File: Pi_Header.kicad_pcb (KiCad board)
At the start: 2 copper layers, 4 parts, among them J1 Raspberry_Pi_2_3, J2 UART, J3 I2C, U1 BD9F800MUX-ZE2

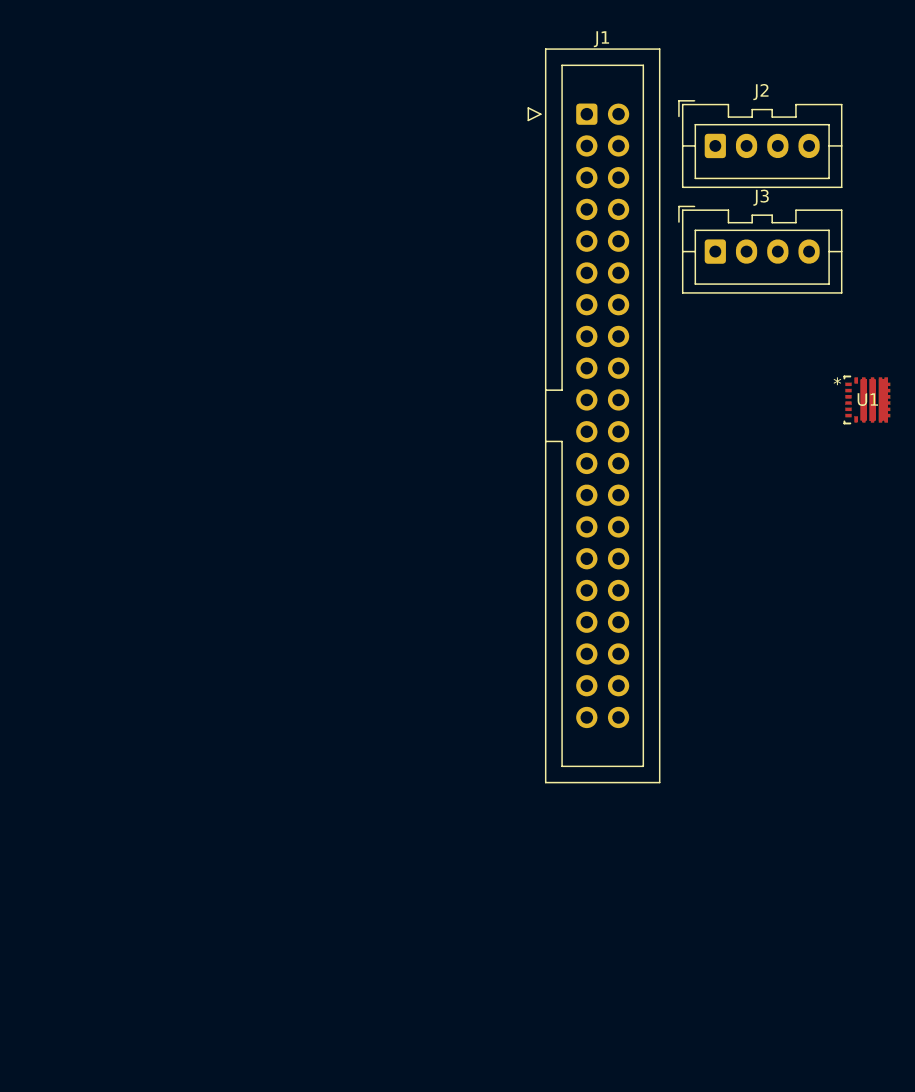
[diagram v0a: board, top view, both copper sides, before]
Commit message: スケッチ完成、PCBベタまで完成　あと外形
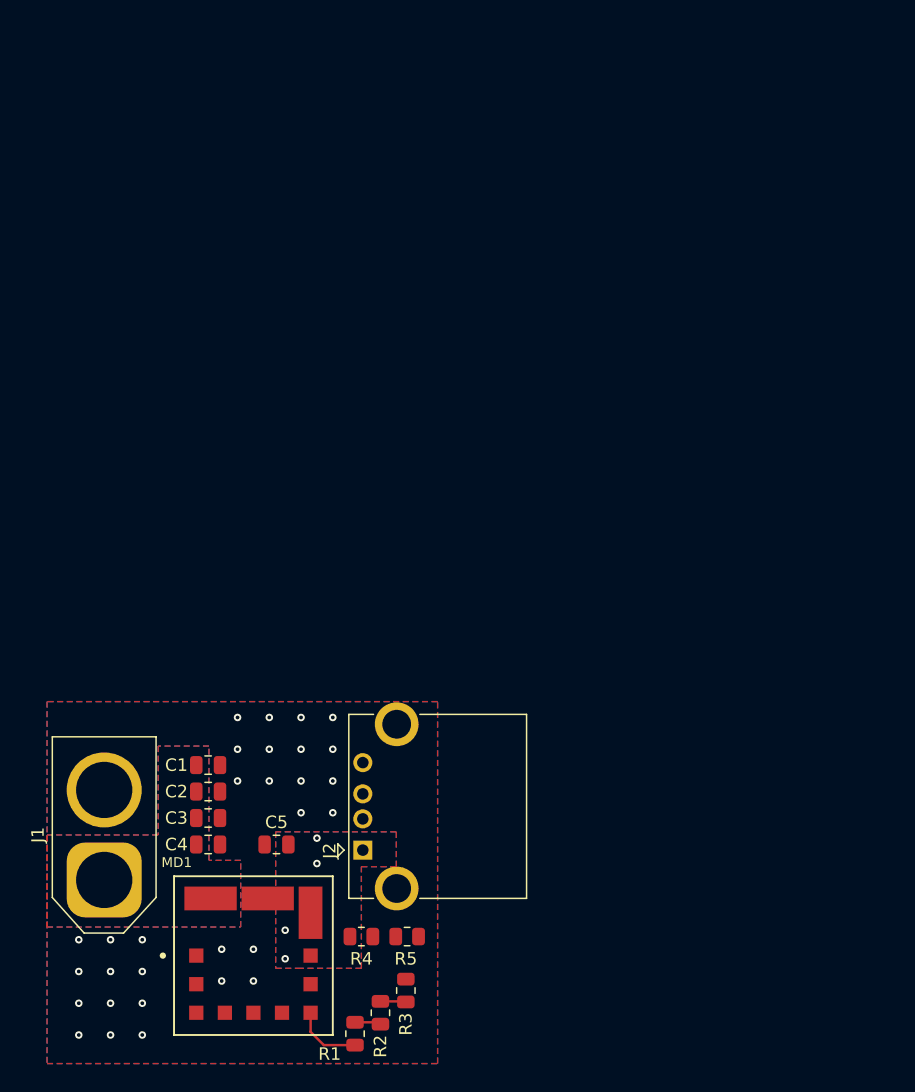
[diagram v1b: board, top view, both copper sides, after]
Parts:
- removed J3: I2C, Connector_JST:JST_XA_B04B-XASK-1_1x04_P2.50mm_Vertical
- removed U1: BD9F800MUX-ZE2, VQFN11_ROM:BD9F800MUX
- added C1: 10uF, Capacitor_SMD:C_0805_2012Metric, F.Cu at (73.8, 64.8)
- added C2: 10uF, Capacitor_SMD:C_0805_2012Metric, F.Cu at (73.8, 66.9)
- added C3: 1uF, Capacitor_SMD:C_0805_2012Metric, F.Cu at (73.8, 69.0)
- added C4: 1uF, Capacitor_SMD:C_0805_2012Metric, F.Cu at (73.8, 71.1)
- added C5: 10uF, Capacitor_SMD:C_0805_2012Metric, F.Cu at (79.3, 71.1)
- added MD1: OKL-T_6-W12N-C, Pi_Header:MURATA_OKL-T-6-W12N-C_0, F.Cu at (77.5, 80.0)
- added R1: 1k, Resistor_SMD:R_0805_2012Metric, F.Cu at (85.6, 86.3)
- added R2: 330R, Resistor_SMD:R_0805_2012Metric, F.Cu at (87.6, 84.6)
- added R3: 10R, Resistor_SMD:R_0805_2012Metric, F.Cu at (89.7, 82.8)
- added R4: 1k, Resistor_SMD:R_0805_2012Metric, F.Cu at (86.1, 78.5)
- added R5: 200R, Resistor_SMD:R_0805_2012Metric, F.Cu at (89.8, 78.5)
- J1: value Raspberry_Pi_2_3 -> PWR_IN; footprint Connector_IDC:IDC-Header_2x20_P2.54mm_Vertical -> Connector_AMASS:AMASS_XT60-M_1x02_P7.20mm_Vertical
- J2: value UART -> USB_A; footprint Connector_JST:JST_XA_B04B-XASK-1_1x04_P2.50mm_Vertical -> Connector_USB:USB_A_CONNFLY_DS1095-WNR0
- moved J1 72.4 mm to (65.5, 74.0), turned to 90 degrees
- moved J2 63.0 mm to (86.2, 71.6), turned to 90 degrees
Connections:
- J1 pad 1: +3V3 -> +BATT
- J1 pad 2: +5V -> GND
- J2 pad 1: TX -> +5V
- J2 pad 2: RX -> unconnected-(J2-D--Pad2)
- J2 pad 3: +5V -> unconnected-(J2-D+-Pad3)
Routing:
- net Net-(MD1-TRIM): track 0.00 -> 5.52 mm
- net Net-(R1-Pad2): track 0.00 -> 2.09 mm
- net Net-(R2-Pad2): track 0.00 -> 2.05 mm
- net GND: vias 0 -> 30
- net +5V: vias 0 -> 4
- added copper zone on B.Cu, net +5V
- added copper zone on F.Cu, net +5V
- added copper zone on B.Cu, net +BATT
- added copper zone on F.Cu, net +BATT
- added copper zone on B.Cu, net GND
- added copper zone on F.Cu, net GND
